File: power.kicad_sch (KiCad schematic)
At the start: 13 parts, among them J34 Conn_01x04, J35 Conn_01x04

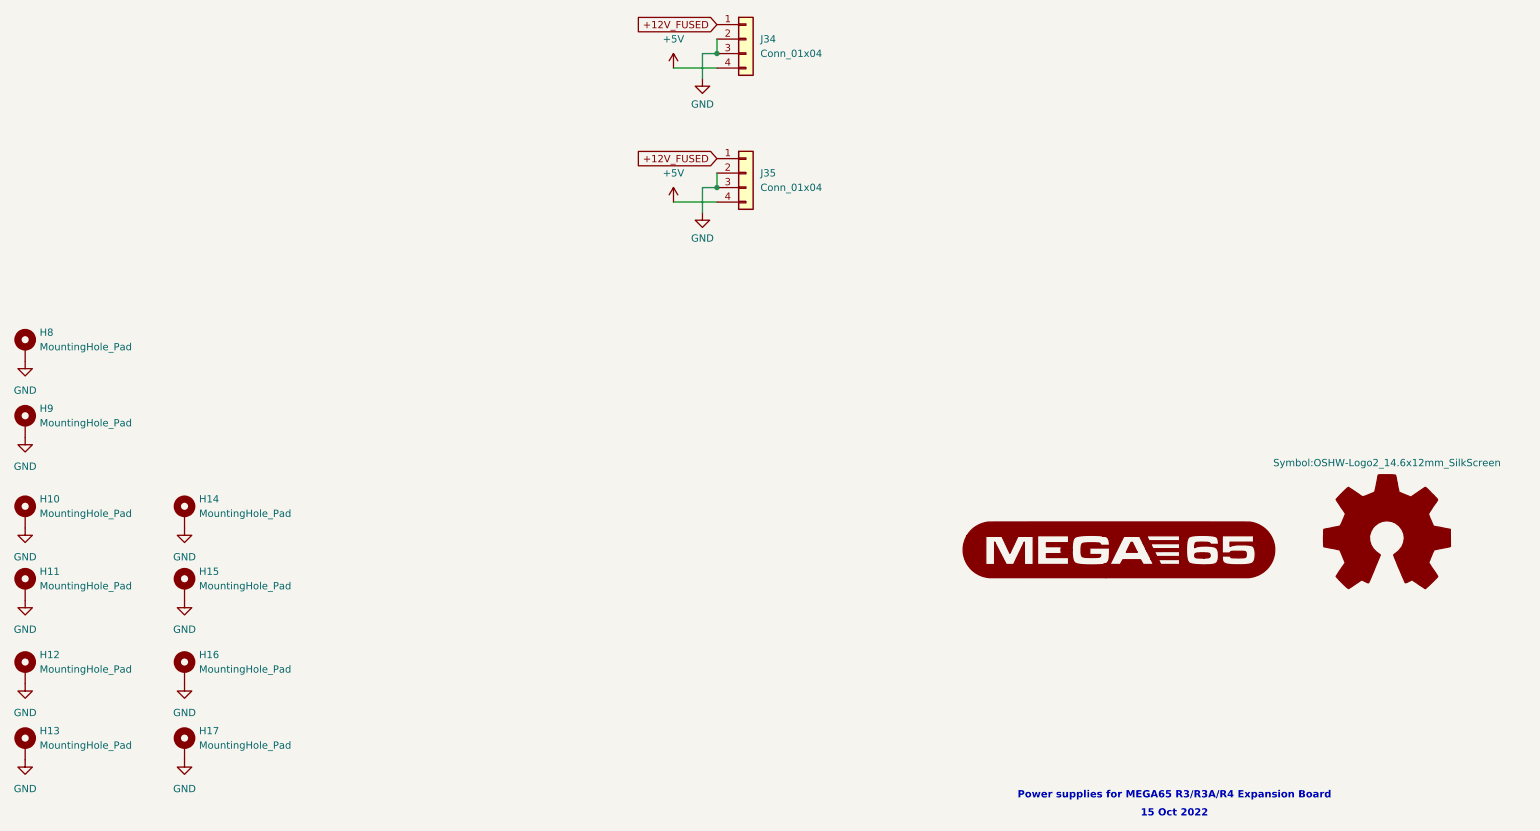
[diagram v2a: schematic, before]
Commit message: work on rerouting board to fit current limiting resistors #1
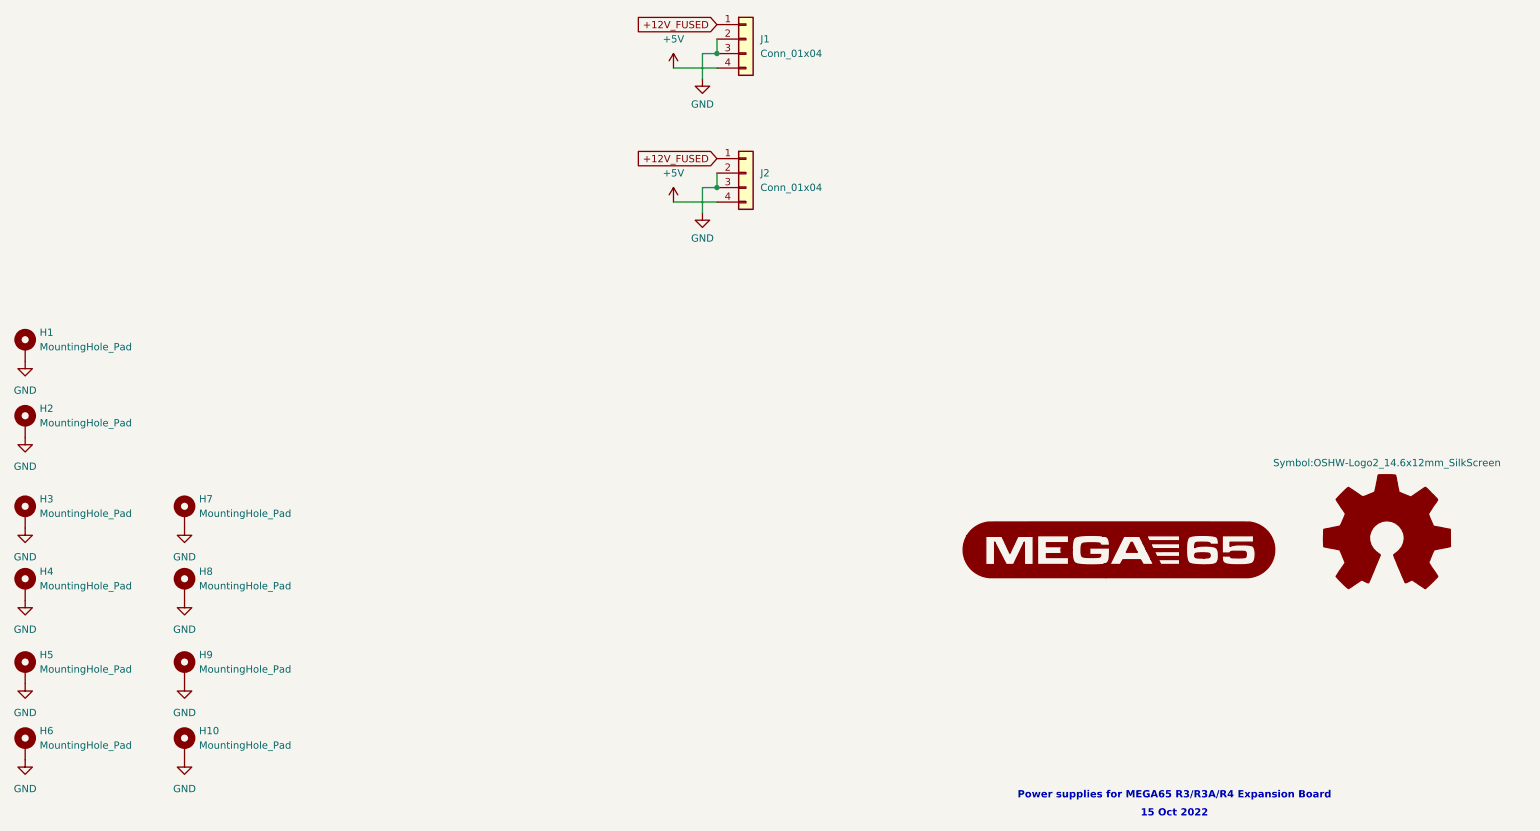
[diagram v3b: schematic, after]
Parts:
- renumbered H8 to H1, H17 to H10, H9 to H2, H10 to H3, H11 to H4, H12 to H5, H13 to H6, H14 to H7, H15 to H8, H16 to H9, J34 to J1, J35 to J2
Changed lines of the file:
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@@
   (symbol (lib_id "power:GND") (at 47.625 143.51 0) (unit 1)
     (in_bom yes) (on_board yes) (fields_autoplaced)
-    (property "Reference" "#PWR0324" (id 0) (at 47.625 149.86 0)
+    (property "Reference" "#PWR07" (id 0) (at 47.625 149.86 0)
       (effects (font (size 1.27 1.27)) hide)
     )
@@
   (symbol (lib_id "Mechanical:MountingHole_Pad") (at 19.685 111.76 0) (unit 1)
     (in_bom yes) (on_board yes) (fields_autoplaced)
-    (property "Reference" "H8" (id 0) (at 22.225 109.2199 0)
+    (property "Reference" "H1" (id 0) (at 22.225 109.2199 0)
       (effects (font (size 1.27 1.27)) (justify left))
     )
@@
   (symbol (lib_id "power:GND") (at 19.685 170.815 0) (unit 1)
     (in_bom yes) (on_board yes) (fields_autoplaced)
-    (property "Reference" "#PWR0320" (id 0) (at 19.685 177.165 0)
+    (property "Reference" "#PWR05" (id 0) (at 19.685 177.165 0)
       (effects (font (size 1.27 1.27)) hide)
     )
@@
   (symbol (lib_id "power:GND") (at 19.685 143.51 0) (unit 1)
     (in_bom yes) (on_board yes) (fields_autoplaced)
-    (property "Reference" "#PWR0325" (id 0) (at 19.685 149.86 0)
+    (property "Reference" "#PWR03" (id 0) (at 19.685 149.86 0)
       (effects (font (size 1.27 1.27)) hide)
     )
@@
   (symbol (lib_id "power:GND") (at 138.43 88.265 0) (unit 1)
     (in_bom yes) (on_board yes) (fields_autoplaced)
-    (property "Reference" "#PWR0340" (id 0) (at 138.43 94.615 0)
+    (property "Reference" "#PWR014" (id 0) (at 138.43 94.615 0)
       (effects (font (size 1.27 1.27)) hide)
     )
@@
   (symbol (lib_id "Connector_Generic:Conn_01x04") (at 146.05 57.785 0) (unit 1)
     (in_bom yes) (on_board yes) (fields_autoplaced)
-    (property "Reference" "J34" (id 0) (at 148.59 57.7849 0)
+    (property "Reference" "J1" (id 0) (at 148.59 57.7849 0)
       (effects (font (size 1.27 1.27)) (justify left))
     )
@@
   (symbol (lib_id "power:GND") (at 19.685 184.15 0) (unit 1)
     (in_bom yes) (on_board yes) (fields_autoplaced)
-    (property "Reference" "#PWR0321" (id 0) (at 19.685 190.5 0)
+    (property "Reference" "#PWR06" (id 0) (at 19.685 190.5 0)
       (effects (font (size 1.27 1.27)) hide)
     )
@@
   (symbol (lib_id "Mechanical:MountingHole_Pad") (at 47.625 181.61 0) (unit 1)
     (in_bom yes) (on_board yes) (fields_autoplaced)
-    (property "Reference" "H17" (id 0) (at 50.165 179.0699 0)
+    (property "Reference" "H10" (id 0) (at 50.165 179.0699 0)
       (effects (font (size 1.27 1.27)) (justify left))
     )
@@
   (symbol (lib_id "Mechanical:MountingHole_Pad") (at 19.685 125.095 0) (unit 1)
     (in_bom yes) (on_board yes) (fields_autoplaced)
-    (property "Reference" "H9" (id 0) (at 22.225 122.5549 0)
+    (property "Reference" "H2" (id 0) (at 22.225 122.5549 0)
       (effects (font (size 1.27 1.27)) (justify left))
     )
@@
   (symbol (lib_id "Mechanical:MountingHole_Pad") (at 47.625 168.275 0) (unit 1)
     (in_bom yes) (on_board yes) (fields_autoplaced)
-    (property "Reference" "H16" (id 0) (at 50.165 165.7349 0)
+    (property "Reference" "H9" (id 0) (at 50.165 165.7349 0)
       (effects (font (size 1.27 1.27)) (justify left))
     )
@@
   (symbol (lib_id "power:GND") (at 138.43 64.77 0) (unit 1)
     (in_bom yes) (on_board yes) (fields_autoplaced)
-    (property "Reference" "#PWR0338" (id 0) (at 138.43 71.12 0)
+    (property "Reference" "#PWR013" (id 0) (at 138.43 71.12 0)
       (effects (font (size 1.27 1.27)) hide)
     )
@@
   (symbol (lib_id "Mechanical:MountingHole_Pad") (at 19.685 168.275 0) (unit 1)
     (in_bom yes) (on_board yes) (fields_autoplaced)
-    (property "Reference" "H12" (id 0) (at 22.225 165.7349 0)
+    (property "Reference" "H5" (id 0) (at 22.225 165.7349 0)
       (effects (font (size 1.27 1.27)) (justify left))
     )
@@
   (symbol (lib_id "Mechanical:MountingHole_Pad") (at 47.625 153.67 0) (unit 1)
     (in_bom yes) (on_board yes) (fields_autoplaced)
-    (property "Reference" "H15" (id 0) (at 50.165 151.1299 0)
+    (property "Reference" "H8" (id 0) (at 50.165 151.1299 0)
       (effects (font (size 1.27 1.27)) (justify left))
     )
@@
   (symbol (lib_id "power:GND") (at 47.625 156.21 0) (unit 1)
     (in_bom yes) (on_board yes) (fields_autoplaced)
-    (property "Reference" "#PWR0323" (id 0) (at 47.625 162.56 0)
+    (property "Reference" "#PWR08" (id 0) (at 47.625 162.56 0)
       (effects (font (size 1.27 1.27)) hide)
     )
@@
   (symbol (lib_id "power:GND") (at 47.625 170.815 0) (unit 1)
     (in_bom yes) (on_board yes) (fields_autoplaced)
-    (property "Reference" "#PWR0327" (id 0) (at 47.625 177.165 0)
+    (property "Reference" "#PWR09" (id 0) (at 47.625 177.165 0)
       (effects (font (size 1.27 1.27)) hide)
     )
@@
   (symbol (lib_id "power:GND") (at 19.685 114.3 0) (unit 1)
     (in_bom yes) (on_board yes) (fields_autoplaced)
-    (property "Reference" "#PWR0309" (id 0) (at 19.685 120.65 0)
+    (property "Reference" "#PWR01" (id 0) (at 19.685 120.65 0)
       (effects (font (size 1.27 1.27)) hide)
     )
@@
   (symbol (lib_id "power:GND") (at 47.625 184.15 0) (unit 1)
     (in_bom yes) (on_board yes) (fields_autoplaced)
-    (property "Reference" "#PWR0328" (id 0) (at 47.625 190.5 0)
+    (property "Reference" "#PWR010" (id 0) (at 47.625 190.5 0)
       (effects (font (size 1.27 1.27)) hide)
     )
@@
   (symbol (lib_id "power:+5V") (at 133.35 62.865 0) (unit 1)
     (in_bom yes) (on_board yes) (fields_autoplaced)
-    (property "Reference" "#PWR0337" (id 0) (at 133.35 66.675 0)
+    (property "Reference" "#PWR011" (id 0) (at 133.35 66.675 0)
       (effects (font (size 1.27 1.27)) hide)
     )
@@
   (symbol (lib_id "Mechanical:MountingHole_Pad") (at 19.685 181.61 0) (unit 1)
     (in_bom yes) (on_board yes) (fields_autoplaced)
-    (property "Reference" "H13" (id 0) (at 22.225 179.0699 0)
+    (property "Reference" "H6" (id 0) (at 22.225 179.0699 0)
       (effects (font (size 1.27 1.27)) (justify left))
     )
@@
   (symbol (lib_id "power:GND") (at 19.685 156.21 0) (unit 1)
     (in_bom yes) (on_board yes) (fields_autoplaced)
-    (property "Reference" "#PWR0326" (id 0) (at 19.685 162.56 0)
+    (property "Reference" "#PWR04" (id 0) (at 19.685 162.56 0)
       (effects (font (size 1.27 1.27)) hide)
     )
@@
   (symbol (lib_id "Mechanical:MountingHole_Pad") (at 19.685 153.67 0) (unit 1)
     (in_bom yes) (on_board yes) (fields_autoplaced)
-    (property "Reference" "H11" (id 0) (at 22.225 151.1299 0)
+    (property "Reference" "H4" (id 0) (at 22.225 151.1299 0)
       (effects (font (size 1.27 1.27)) (justify left))
     )
@@
   (symbol (lib_id "power:GND") (at 19.685 127.635 0) (unit 1)
     (in_bom yes) (on_board yes) (fields_autoplaced)
-    (property "Reference" "#PWR0310" (id 0) (at 19.685 133.985 0)
+    (property "Reference" "#PWR02" (id 0) (at 19.685 133.985 0)
       (effects (font (size 1.27 1.27)) hide)
     )
@@
   (symbol (lib_id "Connector_Generic:Conn_01x04") (at 146.05 81.28 0) (unit 1)
     (in_bom yes) (on_board yes) (fields_autoplaced)
-    (property "Reference" "J35" (id 0) (at 148.59 81.2799 0)
+    (property "Reference" "J2" (id 0) (at 148.59 81.2799 0)
       (effects (font (size 1.27 1.27)) (justify left))
     )
@@
   (symbol (lib_id "Mechanical:MountingHole_Pad") (at 19.685 140.97 0) (unit 1)
     (in_bom yes) (on_board yes) (fields_autoplaced)
-    (property "Reference" "H10" (id 0) (at 22.225 138.4299 0)
+    (property "Reference" "H3" (id 0) (at 22.225 138.4299 0)
       (effects (font (size 1.27 1.27)) (justify left))
     )
@@
   (symbol (lib_id "power:+5V") (at 133.35 86.36 0) (unit 1)
     (in_bom yes) (on_board yes) (fields_autoplaced)
-    (property "Reference" "#PWR0339" (id 0) (at 133.35 90.17 0)
+    (property "Reference" "#PWR012" (id 0) (at 133.35 90.17 0)
       (effects (font (size 1.27 1.27)) hide)
     )
@@
   (symbol (lib_id "Mechanical:MountingHole_Pad") (at 47.625 140.97 0) (unit 1)
     (in_bom yes) (on_board yes) (fields_autoplaced)
-    (property "Reference" "H14" (id 0) (at 50.165 138.4299 0)
-      (effects (font (size 1.27 1.27)) (justify left))
-    )
+    (property "Reference" "H7" (id 0) (at 50.165 138.4299 0)
+      (effects (font (size 1.27 1.27)) (justify left))
+    )
